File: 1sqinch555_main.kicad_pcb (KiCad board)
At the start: 2 copper layers, 25 x 25 mm, 23 parts, among them J1 Conn_01x01, J10 Conn_01x01, J12 Conn_01x01, J14 Conn_01x01, J16 Conn_01x01, J18 Conn_01x01, J2 Conn_01x01, J20 Conn_01x01, J22 Conn_01x01, J24 Conn_01x01, J26 Conn_01x01, J28 Conn_01x01, J3 Conn_01x01, J4 Conn_01x01, J5 Conn_01x01, J6 Conn_01x01, J8 Conn_01x01, U1 LM555, U2 4020

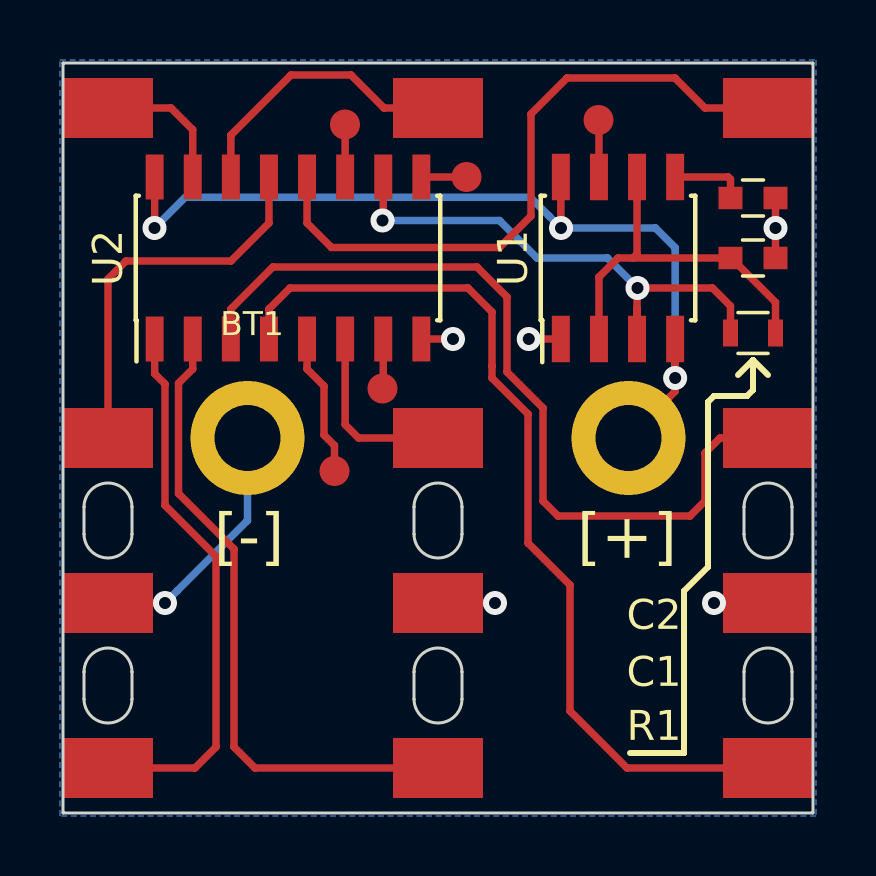
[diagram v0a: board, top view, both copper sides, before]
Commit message: changed 0603 to 0805
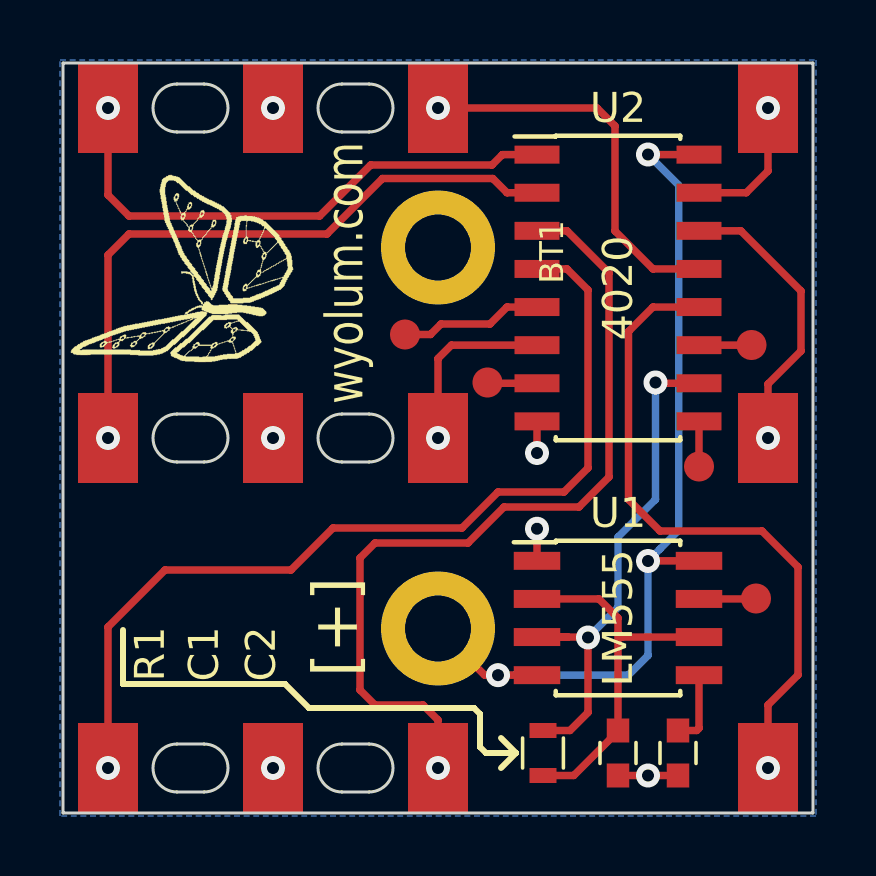
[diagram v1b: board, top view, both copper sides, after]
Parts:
- added G1: Logo-WL3, 1sqinch555_fp:Logo-WL3, F.Cu at (35.2, 46.2)
- moved J12 22.0 mm to (61.0, 61.0), turned to 270 degrees
- moved J16 22.0 mm to (61.0, 39.0), turned to 270 degrees
- moved J18 22.0 mm to (39.0, 39.0), turned to 270 degrees
- moved J6 22.0 mm to (39.0, 61.0), turned to 270 degrees
- moved C2 18.7 mm to (58.0, 60.5), turned to 270 degrees
- moved J26 17.4 mm to (44.5, 39.0), turned to 270 degrees
- moved J28 17.4 mm to (44.5, 61.0), turned to 270 degrees
- moved C1 17.1 mm to (56.0, 60.5), turned to 270 degrees
- moved J1 16.8 mm to (60.6, 55.4), turned to 270 degrees
- moved R1 15.7 mm to (53.5, 60.5), turned to 270 degrees
- moved J10 15.6 mm to (50.0, 39.0), turned to 270 degrees
- moved J14 15.6 mm to (61.0, 50.0), turned to 270 degrees
- moved J20 15.6 mm to (39.0, 50.0), turned to 270 degrees
- moved J22 15.6 mm to (50.0, 61.0), turned to 270 degrees
- moved J4 15.4 mm to (60.5, 46.9), turned to 270 degrees
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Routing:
- net /GND: track 16.4 -> 4.12 mm
- net /Q11: vias 0 -> 1
- net /Q13: vias 0 -> 1
- net /Q12: vias 0 -> 1
- net /Q7: vias 0 -> 1
- net /Q9: vias 0 -> 1
- net /Q8: vias 0 -> 1
- net /Q6: vias 0 -> 1
- net /Q5: vias 0 -> 1
- net /Q10: vias 0 -> 1
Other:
- outline, holes or cut-outs redrawn
- board text added: "wyolum.com"

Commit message: layout changes
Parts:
- added D1: LED, 1sqinch555_fp:LED-0805, F.Cu at (66.2, 55.5)
- added D10: LED, 1sqinch555_fp:LED-0805, F.Cu at (92.7, 55.5)
- added D11: LED, 1sqinch555_fp:LED-0805, F.Cu at (92.7, 47.5)
- added D12: LED, 1sqinch555_fp:LED-0805, F.Cu at (92.7, 39.5)
- added D13: LED, 1sqinch555_fp:LED-0805, F.Cu at (103.5, 55.5)
- added D14: LED, 1sqinch555_fp:LED-0805, F.Cu at (103.5, 47.5)
- added D15: LED, 1sqinch555_fp:LED-0805, F.Cu at (103.5, 39.5)
- added D16: LED, 1sqinch555_fp:LED-0805, F.Cu at (114.3, 55.5)
- added D17: LED, 1sqinch555_fp:LED-0805, F.Cu at (114.3, 47.5)
- added D18: LED, 1sqinch555_fp:LED-0805, F.Cu at (114.3, 39.5)
- added D19: LED, 1sqinch555_fp:LED-0805, F.Cu at (119.2, 55.5)
- added D2: LED, 1sqinch555_fp:LED-0805, F.Cu at (66.2, 47.5)
- added D20: LED, 1sqinch555_fp:LED-0805, F.Cu at (119.2, 47.5)
- added D21: LED, 1sqinch555_fp:LED-0805, F.Cu at (119.2, 39.5)
- added D22: LED, 1sqinch555_fp:LED-0805, F.Cu at (130.0, 55.5)
- added D23: LED, 1sqinch555_fp:LED-0805, F.Cu at (130.0, 47.5)
- added D24: LED, 1sqinch555_fp:LED-0805, F.Cu at (130.0, 39.5)
- added D25: LED, 1sqinch555_fp:LED-0805, F.Cu at (140.8, 55.5)
- added D26: LED, 1sqinch555_fp:LED-0805, F.Cu at (140.8, 47.5)
- added D27: LED, 1sqinch555_fp:LED-0805, F.Cu at (140.8, 39.5)
- added D3: LED, 1sqinch555_fp:LED-0805, F.Cu at (66.2, 39.5)
- added D4: LED, 1sqinch555_fp:LED-0805, F.Cu at (77.0, 55.5)
- added D5: LED, 1sqinch555_fp:LED-0805, F.Cu at (77.0, 47.5)
- added D6: LED, 1sqinch555_fp:LED-0805, F.Cu at (77.0, 39.5)
- added D7: LED, 1sqinch555_fp:LED-0805, F.Cu at (87.8, 55.5)
- added D8: LED, 1sqinch555_fp:LED-0805, F.Cu at (87.8, 47.5)
- added D9: LED, 1sqinch555_fp:LED-0805, F.Cu at (87.8, 39.5)
- added J11: Conn_01x01, 1sqinch555_fp:pad_2x2mm, F.Cu at (88.0, 59.5)
- added J13: Conn_01x01, 1sqinch555_fp:pad_2x2mm, F.Cu at (92.5, 59.5)
- added J15: Conn_01x01, 1sqinch555_fp:pad_2x2mm, F.Cu at (103.5, 59.5)
- added J17: Conn_01x01, 1sqinch555_fp:pad_2x2mm, F.Cu at (114.5, 59.5)
- added J19: Conn_01x01, 1sqinch555_fp:pad_2x2mm, F.Cu at (119.0, 59.5)
- added J21: Conn_01x01, 1sqinch555_fp:pad_2x2mm, F.Cu at (130.0, 59.5)
- added J23: Conn_01x01, 1sqinch555_fp:pad_2x2mm, F.Cu at (141.0, 59.5)
- added J25: Conn_01x01, 1sqinch555_fp:pad_2x2mm, F.Cu at (82.5, 59.5)
- added J27: Conn_01x01, 1sqinch555_fp:pad_2x2mm, F.Cu at (109.0, 59.5)
- added J29: Conn_01x01, 1sqinch555_fp:pad_2x2mm, F.Cu at (135.5, 59.5)
- added J30: Conn_01x01, 1sqinch555_fp:Plated_Hole_d1.0mm, F.Cu at (71.5, 41.0)
- added J31: Conn_01x01, 1sqinch555_fp:Plated_Hole_d1.0mm, F.Cu at (82.5, 41.0)
- added J32: Conn_01x01, 1sqinch555_fp:Plated_Hole_d1.0mm, F.Cu at (98.0, 41.0)
- added J33: Conn_01x01, 1sqinch555_fp:Plated_Hole_d1.0mm, F.Cu at (109.0, 41.0)
- added J34: Conn_01x01, 1sqinch555_fp:Plated_Hole_d1.0mm, F.Cu at (135.5, 41.0)
- added J35: Conn_01x01, 1sqinch555_fp:Plated_Hole_d1.0mm, F.Cu at (124.5, 41.0)
- added J7: Conn_01x01, 1sqinch555_fp:pad_2x2mm, F.Cu at (66.0, 59.5)
- added J9: Conn_01x01, 1sqinch555_fp:pad_2x2mm, F.Cu at (77.0, 59.5)
- added R10: 300, 1sqinch555_fp:R_0805, F.Cu at (137.6, 38.5)
- added R2: 300, 1sqinch555_fp:R_0805, F.Cu at (69.4, 38.5)
- added R3: 300, 1sqinch555_fp:R_0805, F.Cu at (73.8, 38.5)
- added R4: 300, 1sqinch555_fp:R_0805, F.Cu at (84.6, 38.5)
- added R5: 300, 1sqinch555_fp:R_0805, F.Cu at (95.9, 38.5)
- added R6: 300, 1sqinch555_fp:R_0805, F.Cu at (100.3, 38.5)
- added R7: 300, 1sqinch555_fp:R_0805, F.Cu at (111.1, 38.5)
- added R8: 300, 1sqinch555_fp:R_0805, F.Cu at (122.4, 38.5)
- added R9: 300, 1sqinch555_fp:R_0805, F.Cu at (126.8, 38.5)
- added mouse-bite-2.5mm-slot: VAL**, 1sqinch555_fp:mouse-bite-2.5mm-slot, F.Cu at (116.8, 52.8)
- added mouse-bite-2.5mm-slot: VAL**, 1sqinch555_fp:mouse-bite-2.5mm-slot, F.Cu at (116.8, 42.2)
- added mouse-bite-2.5mm-slot: VAL**, 1sqinch555_fp:mouse-bite-2.5mm-slot, F.Cu at (90.2, 52.8)
- added mouse-bite-2.5mm-slot: VAL**, 1sqinch555_fp:mouse-bite-2.5mm-slot, F.Cu at (90.2, 42.2)
- added mouse-bite-2.5mm-slot: VAL**, 1sqinch555_fp:mouse-bite-2.5mm-slot, F.Cu at (63.8, 42.2)
- added mouse-bite-2.5mm-slot: VAL**, 1sqinch555_fp:mouse-bite-2.5mm-slot, F.Cu at (63.8, 52.8)
- C1, C2: footprint 1sqinch555_fp:C_0603 -> 1sqinch555_fp:C_0805
- R1: footprint 1sqinch555_fp:R_0603 -> 1sqinch555_fp:R_0805
- moved C1 11.4 mm to (46.0, 55.0)
- moved R1 11.4 mm to (43.5, 55.0), turned to 90 degrees
- moved G1 4.73 mm to (36.5, 41.6), turned to 0 degrees
- moved C2 0.95 mm to (57.7, 59.6), turned to 180 degrees
- moved J3 0.83 mm to (51.2, 47.5)
- moved J1 0.81 mm to (60.5, 54.5)
- moved U1 0.80 mm to (56.0, 55.2)
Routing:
- net /GND: track 4.12 -> 66.9 mm, vias 6 -> 7
- net /GND3: track 0.00 -> 41.3 mm, vias 0 -> 1
- net /GND2: track 0.00 -> 41.3 mm, vias 0 -> 1
- net /GND1: track 0.00 -> 41.3 mm, vias 0 -> 1
- net /OUT: track 17.9 -> 28.2 mm
- net /Q13: track 28.2 -> 37.6 mm
- net Net-(D8-Pad1): track 0.00 -> 5.90 mm
- net Net-(D7-Pad1): track 0.00 -> 5.90 mm
- net Net-(D5-Pad1): track 0.00 -> 5.90 mm
- net Net-(D4-Pad1): track 0.00 -> 5.90 mm
- net Net-(D26-Pad1): track 0.00 -> 5.90 mm
- net Net-(D25-Pad1): track 0.00 -> 5.90 mm
- net Net-(D23-Pad1): track 0.00 -> 5.90 mm
- net Net-(D22-Pad1): track 0.00 -> 5.90 mm
- net Net-(D20-Pad1): track 0.00 -> 5.90 mm
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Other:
- board size 25 x 25 mm -> 104.5 x 25 mm
- board text added: "1sqinch555"

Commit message: mods
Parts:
- removed D1, D10, D11, D12, D13, D14, D15, D16, D17, D18, D19, D2, D20, D21, D22, D23, D24, D25, D26, D27, D3, D4, D5, D6, D7, D8, D9: LED, 1sqinch555_fp:LED-0805
- removed J11, J13, J15, J17, J19, J21, J23, J25, J27, J29, J7, J9: Conn_01x01, 1sqinch555_fp:pad_2x2mm
- removed J30, J31, J32, J33, J34, J35: Conn_01x01, 1sqinch555_fp:Plated_Hole_d1.0mm
- removed R10, R2, R3, R4, R5, R6, R7, R8, R9: 300, 1sqinch555_fp:R_0805
- removed mouse-bite-2.5mm-slot (x6): VAL**, 1sqinch555_fp:mouse-bite-2.5mm-slot
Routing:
- net /GND3: track 41.3 -> 0.00 mm, vias 1 -> 0
- net /GND2: track 41.3 -> 0.00 mm, vias 1 -> 0
- net /GND1: track 41.3 -> 0.00 mm, vias 1 -> 0
- net Net-(D8-Pad1): track 5.90 -> 0.00 mm
- net Net-(D7-Pad1): track 5.90 -> 0.00 mm
- net Net-(D5-Pad1): track 5.90 -> 0.00 mm
- net Net-(D4-Pad1): track 5.90 -> 0.00 mm
- net Net-(D26-Pad1): track 5.90 -> 0.00 mm
- net Net-(D25-Pad1): track 5.90 -> 0.00 mm
- net Net-(D23-Pad1): track 5.90 -> 0.00 mm
- net Net-(D22-Pad1): track 5.90 -> 0.00 mm
- net Net-(D20-Pad1): track 5.90 -> 0.00 mm
- net Net-(D2-Pad1): track 5.90 -> 0.00 mm
- net Net-(D19-Pad1): track 5.90 -> 0.00 mm
- net Net-(D17-Pad1): track 5.90 -> 0.00 mm
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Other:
- board size 104.5 x 25 mm -> 25 x 25 mm
